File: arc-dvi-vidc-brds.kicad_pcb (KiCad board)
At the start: 4 copper layers, 52.1 x 72 mm, 28 parts, among them IC1 SN74ALVC164245, IC2 SN74ALVC164245, IC3 SN74ALVC164245, J1 Connector_50pin_FFC, U1 MIC5219 3.3V

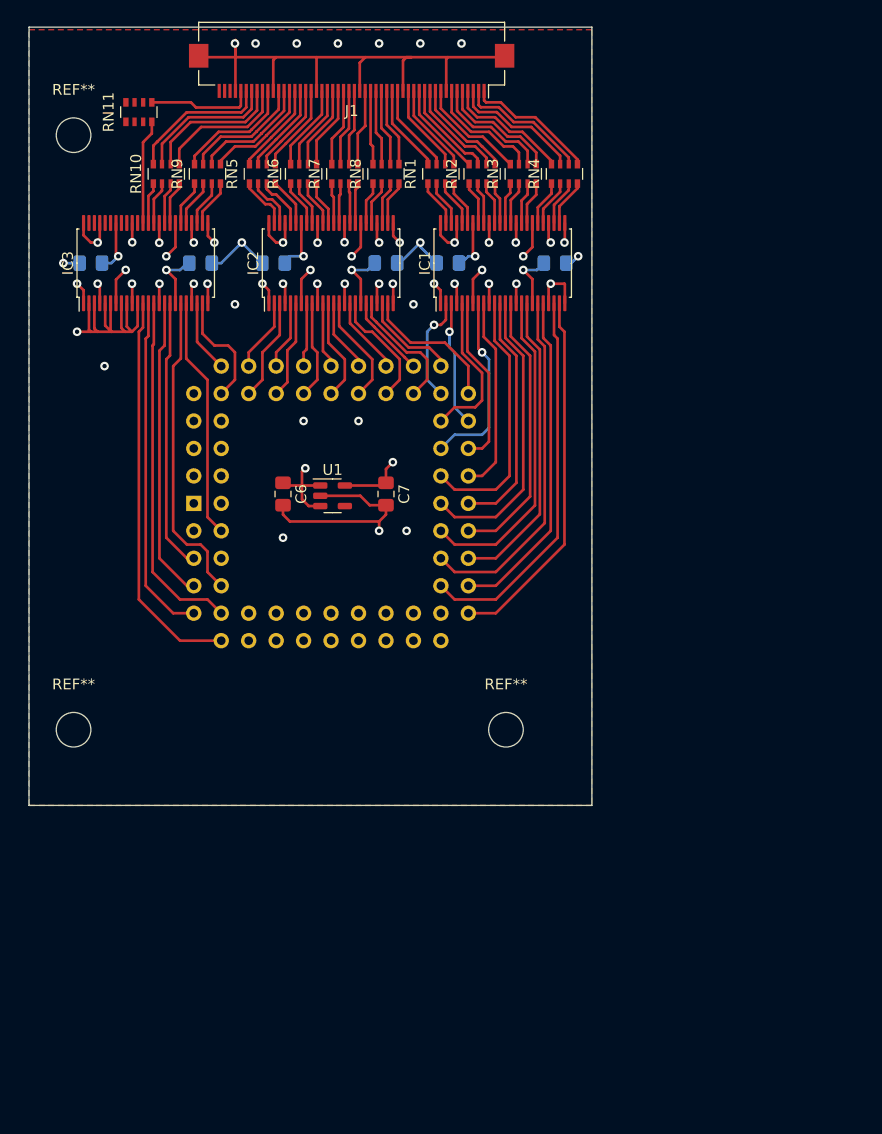
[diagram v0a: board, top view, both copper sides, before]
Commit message: Pretty much finished
Not DRC'd though, FIXME.  Routed, with dimensions measured from
A3000/FDD spacing etc.  Includes extra 80mm holes to mount the
podule board under FDD too.
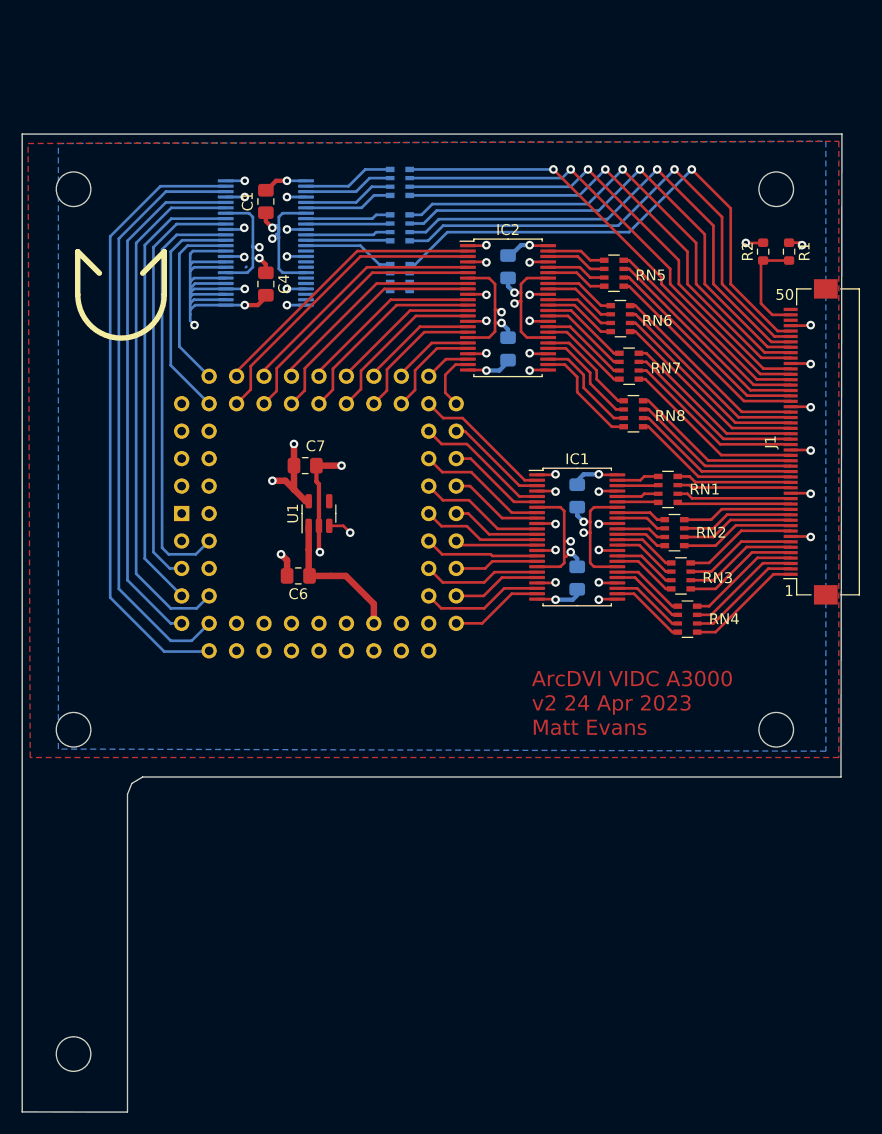
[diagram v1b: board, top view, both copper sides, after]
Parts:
- added R1: 4K7, Resistor_SMD:R_0603_1608Metric, F.Cu at (126.2, 75.8)
- added R2: 4K7, Resistor_SMD:R_0603_1608Metric, F.Cu at (123.8, 75.8)
- added REF**: MountingHole_3.2mm_M3, MountingHole:MountingHole_3.2mm_M3, F.Cu at (60.0, 150.0)
- added REF**: MountingHole_3.2mm_M3, MountingHole:MountingHole_3.2mm_M3, F.Cu at (125.0, 70.0)
- C1, C4: moved to F.Cu
- IC3, RN10, RN11, RN9: moved to B.Cu
- moved J1 54.6 mm to (128.2, 93.4), turned to 90 degrees
- moved RN4 42.7 mm to (116.8, 109.8), turned to 0 degrees
- moved RN3 39.9 mm to (116.2, 105.8), turned to 0 degrees
- moved RN2 37.7 mm to (115.6, 101.8), turned to 0 degrees
- moved RN1 36.0 mm to (115.0, 97.8), turned to 0 degrees
- moved RN5 33.8 mm to (110.0, 77.8), turned to 0 degrees
- moved RN6 32.2 mm to (110.6, 82.0), turned to 0 degrees
- moved RN8 31.9 mm to (111.8, 90.8), turned to 0 degrees
- moved RN7 31.8 mm to (111.4, 86.4), turned to 0 degrees
- moved C8 29.2 mm to (106.6, 106.0), turned to -90 degrees
- moved RN11 28.6 mm to (90.2, 78.2), turned to 0 degrees
- moved IC1 26.3 mm to (106.6, 102.2), turned to 0 degrees
- moved REF** 25.0 mm to (125.0, 120.0)
- moved C3 24.6 mm to (106.6, 98.4), turned to 90 degrees
- moved RN10 22.2 mm to (90.2, 73.6), turned to 0 degrees
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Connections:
- IC3 pad 12: /NVIDW -> /SNDAK
- IC3 pad 13: /NVCS -> /VIDAK
- IC3 pad 14: /NHS -> /CKIN
- IC3 pad 16: /NSNDRQ -> /FLYBK
- IC3 pad 17: /FLYBK -> /NSNDRQ
- IC3 pad 20: /CKIN -> /NVCS
- IC3 pad 22: /SNDAK -> /NHS
- IC3 pad 23: /VIDAK -> /NVIDW
- J1 pad 49: unconnected-(J1-Pad49) -> /ID_DET
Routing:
- net +3V3: track 104.3 -> 242.3 mm, vias 7 -> 9
- net GND: track 317.3 -> 413.7 mm, vias 52 -> 47
- net Net-(J1-Pad46): track 9.88 -> 49.2 mm, vias 0 -> 1
- net +5V: track 133.5 -> 170.5 mm
- net Net-(J1-Pad45): track 13.3 -> 48.0 mm, vias 0 -> 1
- net Net-(J1-Pad44): track 13.2 -> 47.4 mm, vias 0 -> 1
- net Net-(J1-Pad41): track 11.3 -> 45.2 mm, vias 0 -> 1
- net Net-(J1-Pad43): track 13.1 -> 46.8 mm, vias 0 -> 1
- net Net-(J1-Pad42): track 12.5 -> 46.2 mm, vias 0 -> 1
- net Net-(J1-Pad39): track 11.3 -> 44.8 mm, vias 0 -> 1
- net Net-(J1-Pad38): track 11.0 -> 44.3 mm, vias 0 -> 1
- net Net-(J1-Pad37): track 10.5 -> 43.7 mm, vias 0 -> 1
- net /D0: track 34.0 -> 8.62 mm
- net /D1: track 35.5 -> 11.3 mm
- net /D2: track 31.1 -> 8.18 mm
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- added copper zone on B.Cu, net GND
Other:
- board size 52.1 x 72 mm -> 75.8 x 90.5 mm
- board text added: "1"
- board text added: "50"
- board text added: "ArcDVI VIDC A3000 v2 24 Apr 2023 Matt Evans"
- board text added: "FDD holes are spaced 94x70mm"
- board text added: "FDD posts are (centre) 29.5ishmm below PLCC centre"
- board text added: "Links after here, south"
- board text added: "Machine measurements: -- in mm, origin at PLCC centre, where reset sw = north (NOT PCB north) Top posts dia: 10.5 Bottom posts dia: 12 (say 12 all over) - holes 14mm Borders: LK27/bottom border south: 26 Reset sw/top border north: 37 Left posts hole to edge, west: 29 - To centre: 36 Right post hole to edge, east: 51 - To centre: 58 Bottom posts centre south: 29 Top posts centre north: 41"
- board text added: "Main board holes 80mm spacing"
- board text added: "PLCC socket centre is 82.7,100"
- board text added: "Total width of 75mm between FDD posts 25mm from PLCC centre to left 35mm from centre up (avoid reset sw) 50mm from centre right 24mm from centre down to first link, 45 would be reasonable max"
- board text added: "Z: PCB top is 21.2mm beneath FDD bottom plane VIDC is 4.3 tall PTH PLCC68 socket 9.3 tall (i.e. this PCB bottom is 9.3 from mobo top) - a 3M one is 8.0 - Multicomp 8.1 - {dblquote}Standard brand{dblquote} is 8.26 - Adamtech is 8.1 Assuming 8.1 and a 1.6mm PCB, top face is 9.7 from A3K top, or 11.5 below FDD"
- board text removed: "And move regs -- so the stacked variant doesn't need to"
- board text removed: "IC3 needs to move right a bit :("
